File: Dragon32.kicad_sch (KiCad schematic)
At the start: 60 parts, among them IC1 74LS273N, IC10 74LS32N, IC11 74LS123N, IC12 LM1889N, IC13 2318, IC15 MC14053, IC2 MC6847, IC3 74LS00N, IC4 74LS20N, IC5 74LS86AN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

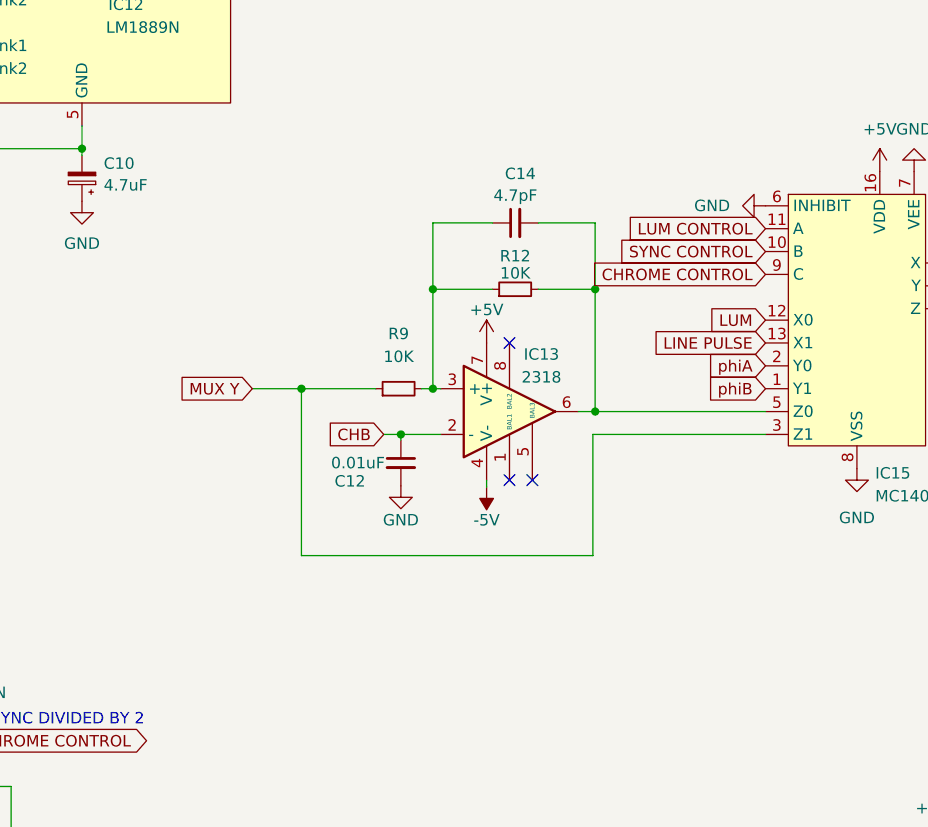
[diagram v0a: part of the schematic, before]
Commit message: fix diff amp wiring
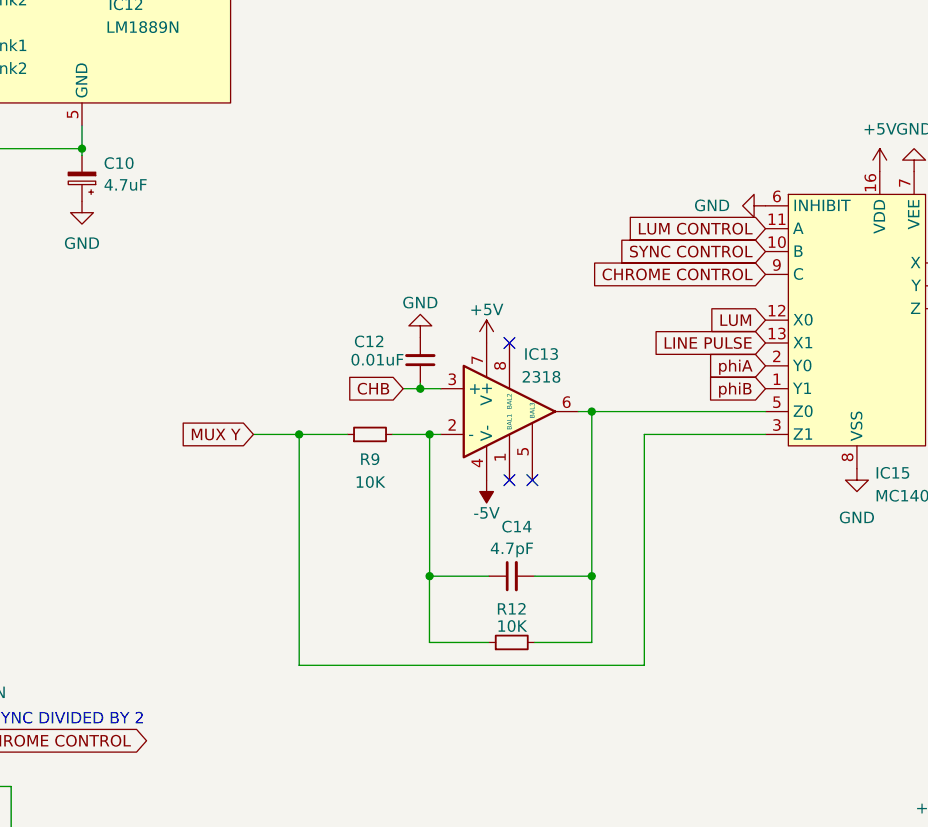
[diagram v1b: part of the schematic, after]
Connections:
- net CHB: now also IC13.3 (+); no longer IC13.2 (-)
- net at C14.1, R12.1, R9.2: now also IC13.2 (-); no longer IC13.3 (+)
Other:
- moved on the sheet: C12, C14, R12, R9

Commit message: move -5v
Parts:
- added C18: 100uF, Capacitor_THT:CP_Radial_D6.3mm_P2.50mm, symbol Device:C_Polarized_Small
- added RN1, RN2: 4K7, Resistor_THT:R_Array_SIP9, symbol Device:R_Network08
- added TP1: TestPoint_LinePulse, TestPoint:TestPoint_Keystone_5000-5004_Miniature, symbol Connector:TestPoint_Small
- added TP2: TestPoint_HS, TestPoint:TestPoint_Keystone_5000-5004_Miniature, symbol Connector:TestPoint_Small
- added TP3, TP4, TP5, TP6: TestPoint_NHS, TestPoint:TestPoint_Keystone_5000-5004_Miniature, symbol Connector:TestPoint_Small
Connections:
- net +5V: now also C18.1, RN1.1 (common)
- net -5V: now also J2.3 (Pin_3); no longer J1.2 (Pin_2)
- net CHROME CONTROL: now also TP6.1
- net CSS: now also RN2.9 (R8)
- net DO0: now also RN1.2 (R1)
- net DO1: now also RN1.5 (R4)
- net DO2: now also RN1.6 (R5)
- net DO3: now also RN1.8 (R7)
- net DO4: now also RN1.9 (R8)
- net DO5: now also RN1.7 (R6)
- net DO6: now also RN1.4 (R3)
- net DO7: now also RN1.3 (R2)
- net GM0: now also RN2.6 (R5)
- net GM1: now also RN2.5 (R4)
- net GM2: now also RN2.4 (R3)
- net GND: now also C18.2, RN2.1 (common)
- net LINE PULSE: now also TP1.1
- net LUM CONTROL: now also TP4.1
- net MUX X: now also R11.2; no longer R11.1
- net SYNC CONTROL: now also TP5.1
- net ~{A}/G: now also RN2.8 (R7)
- net ~{FS}: now also RN2.2 (R1)
- net ~{HS}: now also TP2.1
- net ~{NHS}: now also RN2.3 (R2), TP3.1
- net ~{RAS0}: now also RN2.7 (R6)
- net ~{VCLK}: now also IC5.3, IC7.11 (C); no longer IC3.8, IC8.1 (CP)
- net at R13.2, R14.1, R17.2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: now also R11.1; no longer R11.2
- net D6: now reaches IC1.16 (Q6), IC2.2 (D6), IC2.32 (INV)
- net D0: now reaches IC1.2 (Q0), IC2.3 (D0)
- net D7: now reaches IC1.19 (Q7), IC2.34 (~{A}/S), IC2.40 (D7)
- net D1: now reaches IC1.5 (Q1), IC2.4 (D1)
- net D2: now reaches IC1.6 (Q2), IC2.5 (D2)
- net D3: now reaches IC1.9 (Q3), IC2.6 (D3)
- net D4: now reaches IC1.12 (Q4), IC2.7 (D4)
- net D5: now reaches IC1.15 (Q5), IC2.8 (D5)
- net LINE PULSES renamed HS LINE PULSES
- new net VCLK': IC3.8, IC8.1 (CP)
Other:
- moved on the sheet: C10, C11, C13, C15, C16, C17, C2, C4, C5, C6, C7, C8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

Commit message: trial ATF1504
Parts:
- removed C5: 100pF, Capacitor_THT:C_Disc_D3.0mm_W2.0mm_P2.50mm, symbol Device:C_Small
- removed C9: 180pF, Capacitor_THT:C_Disc_D3.0mm_W2.0mm_P2.50mm, symbol Device:C_Small
- removed IC10: 74LS32N, Package_DIP:DIP-14_W7.62mm, symbol 74xx:74LS32
- removed IC3: 74LS00N, Package_DIP:DIP-14_W7.62mm, symbol 74xx:74LS00
- removed IC4: 74LS20N, Package_DIP:DIP-14_W7.62mm, symbol 74xx:74LS20
- removed IC5: 74LS86AN, Package_DIP:DIP-14_W7.62mm, symbol 74xx:74LS86
- removed IC6, IC8: 74LS393N, Package_DIP:DIP-14_W7.62mm, symbol 74xx:74LS393
- removed IC7: 74ALS74N, Package_DIP:DIP-14_W7.62mm, symbol 74xx:74LS74
- removed IC9: 74LS390, Package_DIP:DIP-16_W7.62mm, symbol 74xx:74LS390
- added U1: ATF1504ASL-xAx44, Package_QFP:TQFP-44_10x10mm_P0.8mm, symbol CPLD_Microchip:ATF1504ASL-xAx44
- C4: value 180pF -> 0.01uF; footprint Capacitor_THT:C_Disc_D3.0mm_W2.0mm_P2.50mm -> Capacitor_THT:C_Disc_D4.3mm_W1.9mm_P5.00mm; DigiKey BC1016CT-ND -> BC2662CT-ND
- R6: value 12K -> 1K8; DigiKey CF14JT15K0CT-ND -> CF14JT10K0CT-ND
- R7: DigiKey CF14JT6K80CT-ND -> CF14JT10K0CT-ND; alt 20K -> (none)
- R8: value 1K8 -> 12K; DigiKey CF14JT3K30CT-ND -> CF14JT10K0CT-ND; alt 2K7 -> (none)
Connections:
- net +5V: now also C4.1, IC11.10 (B), U1.17 (VCC), U1.29 (VCC), U1.41 (VCC), U1.9 (VCC)
- net CHROME CONTROL: now also U1.30 (I/O)
- net CLK: now also U1.42 (I/O)
- net DA0: now also U1.43 (I/O); no longer IC2.22 (DA0)
- net GND: now also IC11.11 (Clr), IC11.6 (Cext), IC11.9 (A), R6.1, U1.16 (GND), U1.24 (GND), U1.36 (GND), U1.4 (GND); no longer R8.1
- net LINE PULSE: now also R6.2; no longer R6.1
- net LUM CONTROL: now also U1.33 (I/O)
- net VCLK: now also U1.3 (I/O)
- net ~{FS}: now also U1.6 (I/O)
- net ~{HS}: now also U1.8 (I/O)
- net ~{NHS}: now also U1.44 (I/O); no longer IC11.2 (B)
- net E: now reaches J1.21 (Pin_21)
- net E: now also U1.10 (I/O)
- net PhaseT: now reaches IC11.4 (~{Q})
- net PhaseT: now also U1.11 (I/O)
- new net Burst: IC11.2 (B), U1.31 (I/O)
- new net DA0': IC2.22 (DA0), U1.2 (I/O)
- new net PadLuma: R8.1, U1.34 (I/O)
- new net TCK: U1.26 (I/O/TCK)
- new net TDI: U1.1 (I/O/TDI)
- new net TDO: U1.32 (I/O/TDO)
- no-connect marks 51 -> 41
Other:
- note removed: "24 LINE DELAY"
- note removed: "DIVIDE BY 50"
- note removed: "DIVIDE VCLK BY 228 TO CREATE LINE PULSE FREQUENCY"
- note removed: "HSYNC DIVIDED BY 2"
- note removed: "OUTPUT LOW ON COUNT 0-15 LINE PULSE WIDTH = 4.5us"
- note removed: "STEER VCLK TO VDG OR LINE PULSE CIRCUIT"
- moved on the sheet: C12, C14, IC11B, IC13, R12, R9

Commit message: provide jtag connections
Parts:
- added C19, C20, C5, C9: 0.1uF, Capacitor_SMD:C_0805_2012Metric_Pad1.18x1.45mm_HandSolder, symbol Device:C_Small
- added J3: JTAG, Connector_PinHeader_1.27mm:PinHeader_2x05_P1.27mm_Vertical, symbol Connector_Generic:Conn_02x05_Odd_Even
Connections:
- net +5V: now also C19.1, C20.1, C5.1, C9.1, J3.4 (Pin_4)
- net GND: now also C19.2, C20.2, C5.2, C9.2, J3.10 (Pin_10), J3.2 (Pin_2)
- net TCK: now also J3.1 (Pin_1)
- net TDI: now also J3.9 (Pin_9)
- net TDO: now also J3.3 (Pin_3)
- net TMS: now reaches U1.7 (I/O/TMS)
- net TMS: now also J3.5 (Pin_5)
- net ~{RESET}: now reaches J1.2 (Pin_2)
- net ~{RESET}: now also J3.6 (Pin_6)
- no-connect marks 41 -> 44

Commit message: revise layout
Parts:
- added TP7: TestPoint_Y, TestPoint:TestPoint_Keystone_5000-5004_Miniature, symbol Connector:TestPoint_Small
- added TP8: TestPoint_C, TestPoint:TestPoint_Keystone_5000-5004_Miniature, symbol Connector:TestPoint_Small
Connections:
- net CSS: now also RN2.8 (R7); no longer RN2.9 (R8)
- net Composite: now also TP8.1
- net GM0: now also RN2.5 (R4); no longer RN2.6 (R5)
- net GM1: now also RN2.4 (R3); no longer RN2.5 (R4)
- net GM2: now also RN2.3 (R2); no longer RN2.4 (R3)
- net MUX X: now also TP7.1
- net ~{A}/G: now also RN2.7 (R6); no longer RN2.8 (R7)
- net ~{FS}: now also RN2.9 (R8); no longer RN2.2 (R1)
- net ~{NHS}: now also RN2.2 (R1); no longer RN2.3 (R2)
- net ~{RAS0}: now also RN2.6 (R5); no longer RN2.7 (R6)
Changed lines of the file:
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@@
     )
   )
+  (global_label "~{NHS}" (shape input) (at 53.34 101.6 90) (fields_autoplaced)
+    (effects (font (size 1.27 1.27)) (justify left))
+    (property "Intersheetrefs" "${INTERSHEET_REFS}" (at 53.34 95.3985 90)
+      (effects (font (size 1.27 1.27)) (justify left) hide)
+    )
+  )
   (global_label "DO2" (shape input) (at 20.828 38.1 180) (fields_autoplaced)
     (effects (font (size 1.27 1.27)) (justify right))
@@
     )
   )
+  (global_label "GM0" (shape input) (at 45.72 101.6 90) (fields_autoplaced)
+    (effects (font (size 1.27 1.27)) (justify left))
+    (property "Intersheetrefs" "${INTERSHEET_REFS}" (at 45.72 95.3381 90)
+      (effects (font (size 1.27 1.27)) (justify left) hide)
+    )
+  )
   (global_label "MUX Y" (shape input) (at 214.884 134.62 180) (fields_autoplaced)
     (effects (font (size 1.27 1.27)) (justify right))
@@
     )
   )
+  (global_label "~{FS}" (shape input) (at 35.56 101.6 90) (fields_autoplaced)
+    (effects (font (size 1.27 1.27)) (justify left))
+    (property "Intersheetrefs" "${INTERSHEET_REFS}" (at 35.56 96.9709 90)
+      (effects (font (size 1.27 1.27)) (justify left) hide)
+    )
+  )
   (global_label "GM1" (shape input) (at 378.46 34.29 0) (fields_autoplaced)
     (effects (font (size 1.27 1.27)) (justify left))
@@
     )
   )
-  (global_label "GM1" (shape input) (at 45.72 101.6 90) (fields_autoplaced)
-    (effects (font (size 1.27 1.27)) (justify left))
-    (property "Intersheetrefs" "${INTERSHEET_REFS}" (at 45.72 95.3381 90)
-      (effects (font (size 1.27 1.27)) (justify right) hide)
-    )
-  )
   (global_label "DA0'" (shape output) (at 109.22 33.02 0) (fields_autoplaced)
     (effects (font (size 1.27 1.27)) (justify left))
@@
     )
   )
-  (global_label "~{NHS}" (shape input) (at 50.8 101.6 90) (fields_autoplaced)
-    (effects (font (size 1.27 1.27)) (justify left))
-    (property "Intersheetrefs" "${INTERSHEET_REFS}" (at 50.8 95.3985 90)
-      (effects (font (size 1.27 1.27)) (justify left) hide)
-    )
-  )
   (global_label "~{A}{slash}G" (shape input) (at 72.009 55.88 180) (fields_autoplaced)
     (effects (font (size 1.27 1.27)) (justify right))
@@
     )
   )
+  (global_label "~{A}{slash}G" (shape input) (at 40.64 101.6 90) (fields_autoplaced)
+    (effects (font (size 1.27 1.27)) (justify left))
+    (property "Intersheetrefs" "${INTERSHEET_REFS}" (at 40.64 95.5799 90)
+      (effects (font (size 1.27 1.27)) (justify right) hide)
+    )
+  )
   (global_label "DO5" (shape input) (at 20.828 45.72 180) (fields_autoplaced)
     (effects (font (size 1.27 1.27)) (justify right))
@@
     )
   )
+  (global_label "~{RAS0}" (shape input) (at 43.18 101.6 90) (fields_autoplaced)
+    (effects (font (size 1.27 1.27)) (justify left))
+    (property "Intersheetrefs" "${INTERSHEET_REFS}" (at 43.18 94.4914 90)
+      (effects (font (size 1.27 1.27)) (justify left) hide)
+    )
+  )
   (global_label "phiB" (shape output) (at 109.22 76.2 0) (fields_autoplaced)
     (effects (font (size 1.27 1.27)) (justify left))
@@
     )
   )
+  (global_label "Composite" (shape input) (at 263.652 218.948 180) (fields_autoplaced)
+    (effects (font (size 1.27 1.27)) (justify right))
+    (property "Intersheetrefs" "${INTERSHEET_REFS}" (at 251.5429 218.948 0)
+      (effects (font (size 1.27 1.27)) (justify right) hide)
+    )
+  )
   (global_label "TDO" (shape output) (at 131.064 230.632 180) (fields_autoplaced)
     (effects (font (size 1.27 1.27)) (justify right))
@@
     )
   )
-  (global_label "GM0" (shape input) (at 43.18 101.6 90) (fields_autoplaced)
-    (effects (font (size 1.27 1.27)) (justify left))
-    (property "Intersheetrefs" "${INTERSHEET_REFS}" (at 43.18 95.3381 90)
-      (effects (font (size 1.27 1.27)) (justify left) hide)
-    )
-  )
   (global_label "CHROME CONTROL" (shape input) (at 301.752 116.84 180) (fields_autoplaced)
     (effects (font (size 1.27 1.27)) (justify right))
@@
     )
   )
+  (global_label "MUX X" (shape input) (at 263.144 213.106 180) (fields_autoplaced)
+    (effects (font (size 1.27 1.27)) (justify right))
+    (property "Intersheetrefs" "${INTERSHEET_REFS}" (at 254.9295 213.106 0)
+      (effects (font (size 1.27 1.27)) (justify right) hide)
+    )
+  )
+  (global_label "CSS" (shape input) (at 38.1 101.6 90) (fields_autoplaced)
+    (effects (font (size 1.27 1.27)) (justify left))
+    (property "Intersheetrefs" "${INTERSHEET_REFS}" (at 38.1 95.58 90)
+      (effects (font (size 1.27 1.27)) (justify right) hide)
+    )
+  )
   (global_label "LINE PULSE" (shape input) (at 262.89 181.61 180) (fields_autoplaced)
     (effects (font (size 1.27 1.27)) (justify right))
@@
     )
   )
-  (global_label "GM2" (shape input) (at 48.26 101.6 90) (fields_autoplaced)
-    (effects (font (size 1.27 1.27)) (justify left))
-    (property "Intersheetrefs" "${INTERSHEET_REFS}" (at 48.26 95.3381 90)
-      (effects (font (size 1.27 1.27)) (justify right) hide)
-    )
-  )
   (global_label "~{NHS}" (shape input) (at 262.89 191.77 180) (fields_autoplaced)
     (effects (font (size 1.27 1.27)) (justify right))
@@
     )
   )
-  (global_label "~{RAS0}" (shape input) (at 40.64 101.6 90) (fields_autoplaced)
-    (effects (font (size 1.27 1.27)) (justify left))
-    (property "Intersheetrefs" "${INTERSHEET_REFS}" (at 40.64 94.4914 90)
-      (effects (font (size 1.27 1.27)) (justify left) hide)
-    )
-  )
   (global_label "DO1" (shape input) (at 20.828 35.56 180) (fields_autoplaced)
     (effects (font (size 1.27 1.27)) (justify right))
@@
     )
   )
-  (global_label "CSS" (shape input) (at 35.56 101.6 90) (fields_autoplaced)
-    (effects (font (size 1.27 1.27)) (justify left))
-    (property "Intersheetrefs" "${INTERSHEET_REFS}" (at 35.56 95.58 90)
-      (effects (font (size 1.27 1.27)) (justify right) hide)
-    )
-  )
   (global_label "VCLK" (shape input) (at 60.706 210.312 180) (fields_autoplaced)
     (effects (font (size 1.27 1.27)) (justify right))
@@
     )
   )
+  (global_label "GM1" (shape input) (at 48.26 101.6 90) (fields_autoplaced)
+    (effects (font (size 1.27 1.27)) (justify left))
+    (property "Intersheetrefs" "${INTERSHEET_REFS}" (at 48.26 95.3381 90)
+      (effects (font (size 1.27 1.27)) (justify right) hide)
+    )
+  )
   (global_label "~{FS}" (shape output) (at 378.46 46.99 0) (fields_autoplaced)
     (effects (font (size 1.27 1.27)) (justify left))
@@
     )
   )
-  (global_label "~{A}{slash}G" (shape input) (at 38.1 101.6 90) (fields_autoplaced)
-    (effects (font (size 1.27 1.27)) (justify left))
-    (property "Intersheetrefs" "${INTERSHEET_REFS}" (at 38.1 95.5799 90)
-      (effects (font (size 1.27 1.27)) (justify right) hide)
-    )
-  )
   (global_label "LEAD" (shape output) (at 134.874 51.816 180) (fields_autoplaced)
     (effects (font (size 1.27 1.27)) (justify right))
@@
     )
   )
-  (global_label "~{FS}" (shape input) (at 53.34 101.6 90) (fields_autoplaced)
-    (effects (font (size 1.27 1.27)) (justify left))
-    (property "Intersheetrefs" "${INTERSHEET_REFS}" (at 53.34 96.9709 90)
-      (effects (font (size 1.27 1.27)) (justify left) hide)
-    )
-  )
   (global_label "phiB" (shape input) (at 189.23 53.34 180) (fields_autoplaced)
     (effects (font (size 1.27 1.27)) (justify right))
@@
     )
   )
+  (global_label "GM2" (shape input) (at 50.8 101.6 90) (fields_autoplaced)
+    (effects (font (size 1.27 1.27)) (justify left))
+    (property "Intersheetrefs" "${INTERSHEET_REFS}" (at 50.8 95.3381 90)
+      (effects (font (size 1.27 1.27)) (justify right) hide)
+    )
+  )
   (global_label "SYNC CONTROL" (shape input) (at 262.89 201.93 180) (fields_autoplaced)
     (effects (font (size 1.27 1.27)) (justify right))
@@
     )
   )
+  (symbol (lib_id "Connector:TestPoint_Small") (at 263.144 213.106 0) (unit 1)
+    (in_bom yes) (on_board yes) (dnp no) (fields_autoplaced)
+    (property "Reference" "TP7" (at 264.414 211.836 0)
+      (effects (font (size 1.27 1.27)) (justify left))
+    )
+    (property "Value" "TestPoint_Y" (at 264.414 214.376 0)
+      (effects (font (size 1.27 1.27)) (justify left))
+    )
+    (property "Footprint" "TestPoint:TestPoint_Keystone_5000-5004_Miniature" (at 268.224 213.106 0)
+      (effects (font (size 1.27 1.27)) hide)
+    )
+    (property "Datasheet" "~" (at 268.224 213.106 0)
+      (effects (font (size 1.27 1.27)) hide)
+    )
+    (pin "1")
+    (instances
+      (project "Dragon32"
+        (path "/0c3dceba-7c95-4b3d-b590-0eb581444beb"
+          (reference "TP7") (unit 1)
+        )
+      )
+    )
+  )
   (symbol (lib_id "Device:R_Small") (at 243.586 157.734 90) (unit 1)
     (in_bom yes) (on_board yes) (dnp no)
@@
         )
       )
+    )
+  )
+  (symbol (lib_id "Connector:TestPoint_Small") (at 263.652 218.948 0) (unit 1)
+    (in_bom yes) (on_board yes) (dnp no) (fields_autoplaced)
+    (property "Reference" "TP8" (at 264.922 217.678 0)
+      (effects (font (size 1.27 1.27)) (justify left))
+    )
+    (property "Value" "TestPoint_C" (at 264.922 220.218 0)
+      (effects (font (size 1.27 1.27)) (justify left))
+    )
+    (property "Footprint" "TestPoint:TestPoint_Keystone_5000-5004_Miniature" (at 268.732 218.948 0)
+      (effects (font (size 1.27 1.27)) hide)
+    )
+    (property "Datasheet" "~" (at 268.732 218.948 0)
+      (effects (font (size 1.27 1.27)) hide)
+    )
+    (pin "1")
+    (instances
+      (project "Dragon32"
+        (path "/0c3dceba-7c95-4b3d-b590-0eb581444beb"
+          (reference "TP8") (unit 1)
+        )
+      )
